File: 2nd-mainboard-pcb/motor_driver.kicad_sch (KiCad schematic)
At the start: 1 part

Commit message: added libraries
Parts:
- added J15: Stepper Motor, symbol Connector:Conn_01x04_Pin
- added J2: Servo Motor, symbol Connector:Conn_01x03_Socket
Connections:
- net GND: now reaches A1.1 (GND)
- net GND: now also A1.7 (GND)
- net +5V: now reaches A1.13 (~{RST})
- net +5V: now also A1.14 (~{SLP})
- net STEP: now reaches A1.15 (STEP)
- net DIR: now reaches A1.16 (DIR)
- net at A1.3 (A2): now also J15.3 (Pin_3)
- net at A1.4 (A1): now also J15.4 (Pin_4)
- net at A1.5 (B1): now also J15.2 (Pin_2)
- net at A1.6 (B2): now also J15.1 (Pin_1)
- net +12V: now reaches A1.8 (VMOT)
- no-connect marks 0 -> 2

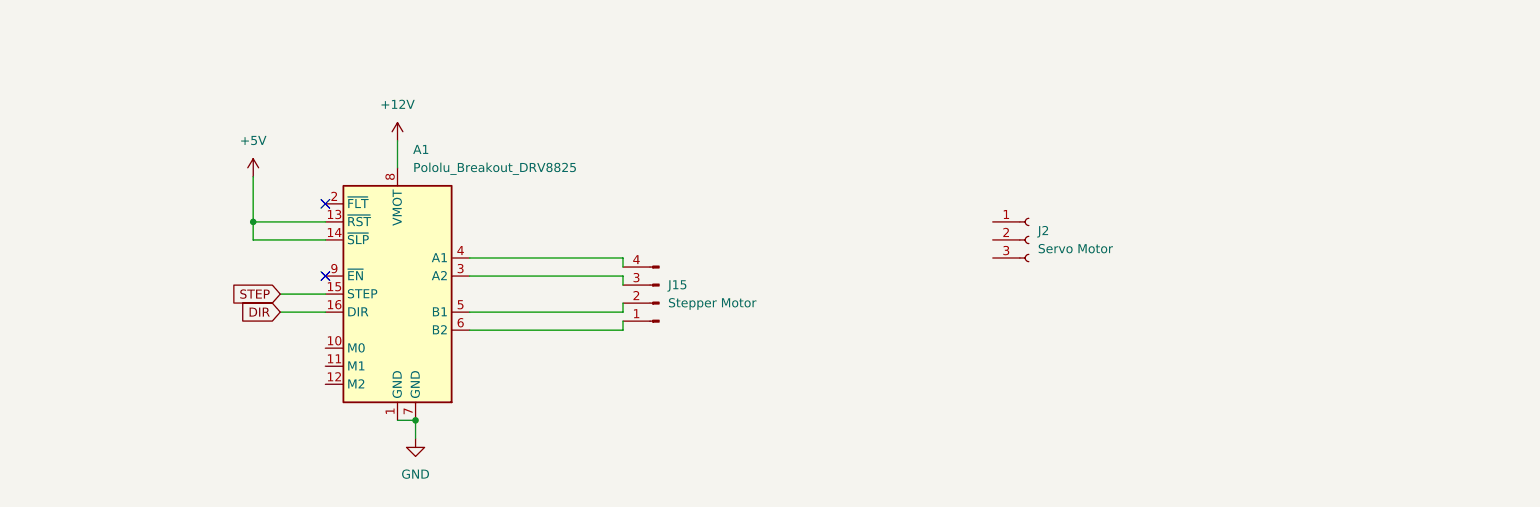
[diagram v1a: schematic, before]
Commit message: added imported components, changed structure
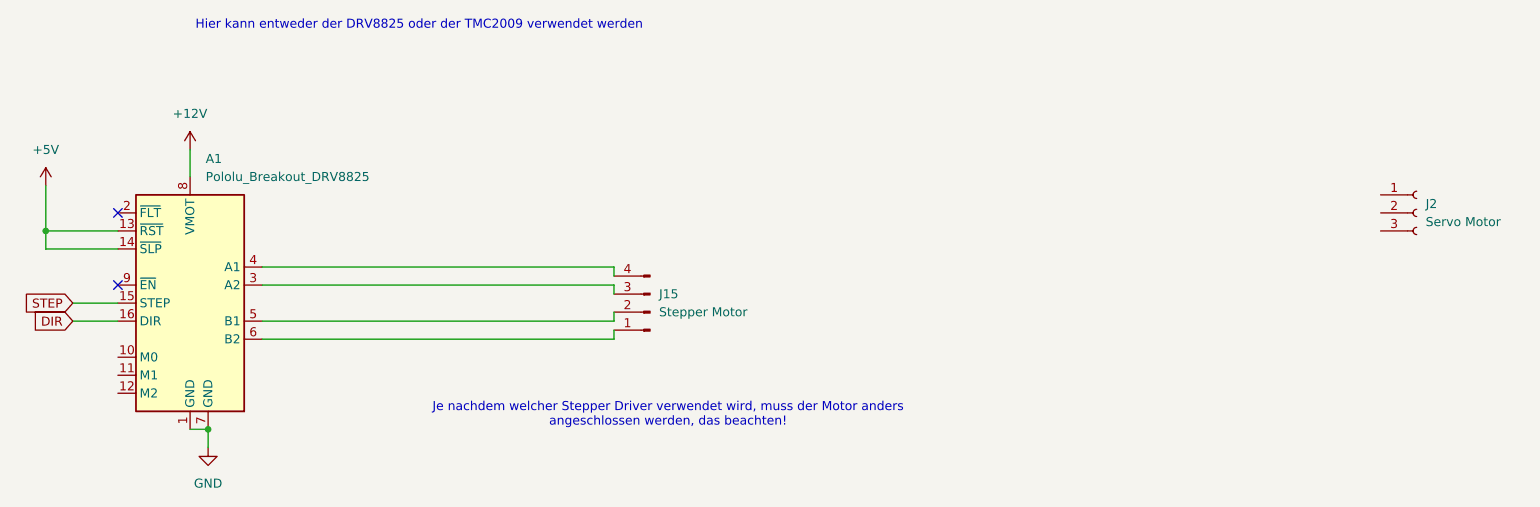
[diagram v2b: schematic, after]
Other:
- note added: "Hier kann entweder der DRV8825 oder der TMC2009 verwendet werden"
- note added: "Je nachdem welcher Stepper Driver verwendet wird, muss der Motor anders angeschlossen werden, das beachten!"
- moved on the sheet: A1, J15, J2

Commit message: Excel überarbeitet
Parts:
- added U4: MPU-6050, Sensor_Motion:InvenSense_QFN-24_4x4mm_P0.5mm, symbol Sensor_Motion:MPU-6050
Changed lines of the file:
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@@
+	)
+	(symbol
+		(lib_id "Sensor_Motion:MPU-6050")
+		(at 62.3888 139.1598 0)
+		(unit 1)
+		(exclude_from_sim no)
+		(in_bom yes)
+		(on_board yes)
+		(dnp no)
+		(fields_autoplaced yes)
+		(property "Reference" "U4"
+			(at 64.5829 155.6698 0)
+			(effects
+				(font
+					(size 1.27 1.27)
+				)
+				(justify left)
+			)
+		)
+		(property "Value" "MPU-6050"
+			(at 64.5829 158.2098 0)
+			(effects
+				(font
+					(size 1.27 1.27)
+				)
+				(justify left)
+			)
+		)
+		(property "Footprint" "Sensor_Motion:InvenSense_QFN-24_4x4mm_P0.5mm"
+			(at 62.3888 159.4798 0)
+			(effects
+				(font
+					(size 1.27 1.27)
+				)
+				(hide yes)
+			)
+		)
+		(property "Datasheet" "https://invensense.tdk.com/wp-content/uploads/2015/02/MPU-6000-Datasheet1.pdf"
+			(at 62.3888 142.9698 0)
+			(effects
+				(font
+					(size 1.27 1.27)
+				)
+				(hide yes)
+			)
+		)
+		(property "Description" "InvenSense 6-Axis Motion Sensor, Gyroscope, Accelerometer, I2C"
+			(at 62.3888 139.1598 0)
+			(effects
+				(font
+					(size 1.27 1.27)
+				)
+				(hide yes)
+			)
+		)
+		(pin "10"
+		)
+		(pin "14"
+		)
+		(pin "18"
+		)
+		(pin "20"
+		)
+		(pin "4"
+		)
+		(pin "5"
+		)
+		(pin "9"
+		)
+		(pin "12"
+		)
+		(pin "17"
+		)
+		(pin "2"
+		)
+		(pin "19"
+		)
+		(pin "7"
+		)
+		(pin "13"
+		)
+		(pin "24"
+		)
+		(pin "11"
+		)
+		(pin "3"
+		)
+		(pin "21"
+		)
+		(pin "8"
+		)
+		(pin "16"
+		)
+		(pin "22"
+		)
+		(pin "6"
+		)
+		(pin "1"
+		)
+		(pin "15"
+		)
+		(pin "23"
+		)
+		(instances
+			(project "2nd-mainboard-pcb"
+				(path "/6926a609-8b92-4b3a-88c8-3d023174b977/14240b98-f570-417b-af10-6e4a6547c4a4"
+					(reference "U4")
+					(unit 1)
+				)
+			)
+		)
 	)
 	(symbol

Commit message: finished stacked design, annotaded
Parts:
- removed J2: Servo Motor, symbol Connector:Conn_01x03_Socket
- added C27, C29, C31: 100nF, symbol Device:C
- added C28, C30: 4.7uF, symbol Device:C_Polarized
- added J12: Microstepping, symbol Connector_Generic:Conn_02x03_Counter_Clockwise
- added J14: Servo Motor SM, Imported_Component_Footprints:JST_XH_S3B-XH-A_1x03_P2.50mm_Horizontal, symbol Connector:Conn_01x03_Pin
- added J15: Servo Motor BL Touch, symbol Connector:Conn_01x03_Pin
- added J16: Conn_01x02_Pin, symbol Connector:Conn_01x02_Pin
- added U12: TMC2209_SILENTSTEPSTICK, Imported_Component_Footprints:MODULE_TMC2209_SILENTSTEPSTICK, symbol Imported_Component_Symbols:TMC2209_SILENTSTEPSTICK
- J13: renamed from J15; footprint (none) -> Imported_Component_Footprints:JST_S4B-XH-A-1
- renumbered U4 to U11
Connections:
- net +12V: now also U12.8 (VM)
- net DIR: now also U12.9 (DIR)
- net GND: now also U11.18 (GND), C27.2, C28.2, C29.2, C30.2, C31.2, J16.1 (Pin_1), U12.1 (GND), U12.7 (GND)
- net STEP: now also U12.10 (STEP)
- net M0: now reaches A1.10 (M0)
- net M0: now also J12.6 (Pin_6)
- net M1: now reaches A1.11 (M1)
- net M1: now also J12.5 (Pin_5), U12.15 (MS1)
- net M2: now reaches A1.12 (M2)
- net M2: now also J12.4 (Pin_4), U12.14 (MS2)
- net STP_A2: now reaches A1.3 (A2), J13.3 (Pin_3)
- net STP_A2: now also U12.5 (M2A)
- net STP_A1: now reaches A1.4 (A1), J13.4 (Pin_4)
- net STP_A1: now also U12.4 (M1A)
- net STP_B1: now reaches A1.5 (B1), J13.2 (Pin_2)
- net STP_B1: now also U12.3 (M1B)
- net STP_B2: now reaches A1.6 (B2), J13.1 (Pin_1)
- net STP_B2: now also U12.6 (M2B)
- net +5V_POW: now reaches U11.13 (VDD)
- net +5V_POW: now also U11.8 (VLOGIC), C27.1, C28.1, C29.1, C30.1, C31.1, J12.1 (Pin_1), J12.2 (Pin_2), J12.3 (Pin_3), J14.2 (Pin_2), J15.2 (Pin_2), U12.2 (VIO)
- net SCL: now reaches U11.23 (SCL)
- net SDA: now reaches U11.24 (SDA)
- new net BLT_Servo: J15.3 (Pin_3)
- new net BLT_Switch: J16.2 (Pin_2)
- new net SM_Servo: J14.3 (Pin_3)
- no-connect marks 2 -> 13
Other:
- note added: "Microstepping mit einem Jumper auf der Platine einstellen"
- note added: "Pinout https://www.studiopieters.nl/drv8825-pinout/"
- note added: "Welcher Pin muss zu UART verbunden werden?! https://www.ic-components.com/blog/your-guide-to-tmc2209-stepper-driver-with-microcontroller.jsp"
- moved on the sheet: J13, U11

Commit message: alle bauteile hinzugefügt
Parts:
- removed J12: Microstepping, symbol Connector_Generic:Conn_02x03_Counter_Clockwise
- added C28, C31: 100nF, Capacitor_SMD:C_0402_1005Metric_Pad0.74x0.62mm_HandSolder, symbol Device:C
- added J14: Microstepping, Imported_Component_Footprints:FTSH-103-01-L-DH, symbol Imported_Component_Symbols:FTSH-103-01-L-DH
- C29: renamed from C28; footprint (none) -> Capacitor_SMD:C_0805_2012Metric_Pad1.18x1.45mm_HandSolder
- C30: renamed from C29; footprint (none) -> Capacitor_SMD:C_0402_1005Metric_Pad0.74x0.62mm_HandSolder
- C32: renamed from C30; footprint (none) -> Capacitor_SMD:C_0805_2012Metric_Pad1.18x1.45mm_HandSolder
- C33: renamed from C31; footprint (none) -> Capacitor_SMD:C_0402_1005Metric_Pad0.74x0.62mm_HandSolder
- C34: renamed from C27; footprint (none) -> Capacitor_SMD:C_0402_1005Metric_Pad0.74x0.62mm_HandSolder
- J13: renamed from J15; now left out of the parts list
- J15: renamed from J16; now left out of the parts list
- U11: renamed from U12; now left out of the parts list
- renumbered J14 to J11, J13 to J12, U11 to U12
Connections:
- net +5V is gone; now on net +5V_POW: A1.13 (~{RST}), A1.14 (~{SLP})
- net +12V: now also C28.1
- net +5V_POW: now also C31.1, J14.01, J14.03, J14.05
- net GND: now also J11.1 (Pin_1), J13.1 (Pin_1), C28.2, C31.2
- net M0: now also J14.02
- net M1: now also J14.04
- net M2: now also J14.06
- net STP_A1: no longer U11.4 (M1A)
- net STP_A2: no longer U11.5 (M2A)
- net STP_B1: no longer U11.3 (M1B)
- net STP_B2: no longer U11.6 (M2B)
- no-connect marks 13 -> 24
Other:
- moved on the sheet: C34, U12

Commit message: mehr positioning
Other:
- moved on the sheet: C29, C30, C34, J11, J12, J14, U12

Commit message: Fan-PCB-Beginning
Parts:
- renumbered C28 to C23, C31 to C24, C29 to C25, C30 to C26, C34 to C27, C32 to C28, C33 to C29, J13 to J10, J15 to J11, J12 to J7, J11 to J8, J14 to J9

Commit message: Motoren Design finished
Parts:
- removed J11: Conn_01x02_Pin, symbol Connector:Conn_01x02_Pin
- added J11: T3, Imported_Component_Footprints:665102131822, symbol Imported_Component_Symbols:665102131822
- C28, C29: now fitted
- J10: footprint (none) -> Imported_Component_Footprints:JST_XH_S3B-XH-A_1x03_P2.50mm_Horizontal; now fitted; now in the parts list
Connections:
- net BLT_Switch: now also J11.2
- net GND: now also J11.1
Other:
- note added: "BL Touch Endschalter"
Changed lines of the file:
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@@
 		)
 	)
+	(text "BL Touch Endschalter"
+		(exclude_from_sim no)
+		(at 260.858 147.828 0)
+		(effects
+			(font
+				(size 1.27 1.27)
+			)
+		)
+	)
 	(global_label "M2"
 		(shape input)
@@
 		(in_bom yes)
 		(on_board yes)
-		(dnp yes)
+		(dnp no)
 		(fields_autoplaced yes)
 		(property "Reference" "#PWR067"
@@
 		(in_bom yes)
 		(on_board yes)
-		(dnp yes)
+		(dnp no)
 		(fields_autoplaced yes)
 		(property "Reference" "C29"
@@
 	)
 	(symbol
+		(lib_id "Imported_Component_Symbols:665102131822")
+		(at 251.46 153.67 270)
+		(unit 1)
+		(exclude_from_sim no)
+		(in_bom yes)
+		(on_board yes)
+		(dnp no)
+		(fields_autoplaced yes)
+		(property "Reference" "J11"
+			(at 252.73 152.3999 90)
+			(effects
+				(font
+					(size 1.27 1.27)
+				)
+				(justify left)
+			)
+		)
+		(property "Value" "T3"
+			(at 260.604 153.924 0)
+			(effects
+				(font
+					(size 1.27 1.27)
+				)
+				(justify bottom)
+				(hide yes)
+			)
+		)
+		(property "Footprint" "Imported_Component_Footprints:665102131822"
+			(at 260.604 153.924 0)
+			(effects
+				(font
+					(size 1.27 1.27)
+				)
+				(justify bottom)
+				(hide yes)
+			)
+		)
+		(property "Datasheet" ""
+			(at 251.46 153.67 0)
+			(effects
+				(font
+					(size 1.27 1.27)
+				)
+				(hide yes)
+			)
+		)
+		(property "Description" ""
+			(at 251.46 153.67 0)
+			(effects
+				(font
+					(size 1.27 1.27)
+				)
+				(hide yes)
+			)
+		)
+		(property "CONTACT-RESISTANCE" "20mOhm"
+			(at 260.604 153.924 0)
+			(effects
+				(font
+					(size 1.27 1.27)
+				)
+				(justify bottom)
+				(hide yes)
+			)
+		)
+		(property "GENDER" "Male"
+			(at 260.604 153.924 0)
+			(effects
+				(font
+					(size 1.27 1.27)
+				)
+				(justify bottom)
+				(hide yes)
+			)
+		)
+		(property "MOUNT" "SMT"
+			(at 254.254 153.416 0)
+			(effects
+				(font
+					(size 1.27 1.27)
+				)
+				(justify bottom)
+				(hide yes)
+			)
+		)
+		(property "IR" "1A"
+			(at 252.73 157.988 0)
+			(effects
+				(font
+					(size 1.27 1.27)
+				)
+				(justify bottom)
+				(hide yes)
+			)
+		)
+		(property "L" "4mm"
+			(at 260.604 153.924 0)
+			(effects
+				(font
+					(size 1.27 1.27)
+				)
+				(justify bottom)
+				(hide yes)
+			)
+		)
+		(property "PACKAGING" "Tape and Reel"
+			(at 260.604 153.924 0)
+			(effects
+				(font
+					(size 1.27 1.27)
+				)
+				(justify bottom)
+				(hide yes)
+			)
+		)
+		(property "PART-NUMBER" "665102131822"
+			(at 260.604 153.924 0)
+			(effects
+				(font
+					(size 1.27 1.27)
+				)
+				(justify bottom)
+				(hide yes)
+			)
+		)
+		(property "DATASHEET-URL" "https://www.we-online.com/redexpert/spec/665102131822?ae"
+			(at 255.778 149.352 0)
+			(effects
+				(font
+					(size 1.27 1.27)
+				)
+				(justify bottom)
+				(hide yes)
+			)
+		)
+		(property "WORKING-VOLTAGE" "50V(AC)"
+			(at 260.604 153.924 0)
+			(effects
+				(font
+					(size 1.27 1.27)
+				)
+				(justify bottom)
+				(hide yes)
+			)
+		)
+		(property "PINS" "2"
+			(at 253.238 150.368 0)
+			(effects
+				(font
+					(size 1.27 1.27)
+				)
+				(justify bottom)
+				(hide yes)
+			)
+		)
+		(property "PITCH" "1mm"
+			(at 260.604 153.924 0)
+			(effects
+				(font
+					(size 1.27 1.27)
+				)
+				(justify bottom)
+				(hide yes)
+			)
+		)
+		(property "TYPE" "Horizontal"
+			(at 260.604 153.924 0)
+			(effects
+				(font
+					(size 1.27 1.27)
+				)
+				(justify bottom)
+				(hide yes)
+			)
+		)
+		(property "PCB-CABLE-PANEL" "PCB"
+			(at 252.222 153.67 0)
+			(effects
+				(font
+					(size 1.27 1.27)
+				)
+				(justify bottom)
+				(hide yes)
+			)
+		)
+		(pin "1"
+		)
+		(pin "2"
+		)
+		(instances
+			(project "2nd-mainboard-pcb"
+				(path "/6926a609-8b92-4b3a-88c8-3d023174b977/14240b98-f570-417b-af10-6e4a6547c4a4"
+					(reference "J11")
+					(unit 1)
+				)
+			)
+		)
+	)
+	(symbol
 		(lib_id "Connector:Conn_01x03_Pin")
 		(at 251.46 123.19 180)
 		(unit 1)
 		(exclude_from_sim no)
-		(in_bom no)
-		(on_board no)
-		(dnp yes)
+		(in_bom yes)
+		(on_board yes)
+		(dnp no)
 		(property "Reference" "J10"
 			(at 252.73 121.9199 0)
@@
 			)
 		)
-		(property "Footprint" ""
+		(property "Footprint" "Imported_Component_Footprints:JST_XH_S3B-XH-A_1x03_P2.50mm_Horizontal"
 			(at 251.46 123.19 0)
 			(effects
@@
 		(in_bom yes)
 		(on_board yes)
-		(dnp yes)
+		(dnp no)
 		(property "Reference" "#PWR066"
 			(at 203.2 143.51 0)
@@
 	)
 	(symbol
-		(lib_id "Connector:Conn_01x02_Pin")
-		(at 251.46 153.67 180)
-		(unit 1)
-		(exclude_from_sim no)
-		(in_bom no)
-		(on_board no)
-		(dnp yes)
-		(fields_autoplaced yes)
-		(property "Reference" "J11"
-			(at 252.73 151.1299 0)
-			(effects
-				(font
-					(size 1.27 1.27)
-				)
-				(justify right)
-			)
-		)
-		(property "Value" "Conn_01x02_Pin"
-			(at 252.73 153.6699 0)
-			(effects
-				(font
-					(size 1.27 1.27)
-				)
-				(justify right)
-			)
-		)
-		(property "Footprint" ""
-			(at 251.46 153.67 0)
-			(effects
-				(font
-					(size 1.27 1.27)
-				)
-				(hide yes)
-			)
-		)
-		(property "Datasheet" "~"
-			(at 251.46 153.67 0)
-			(effects
-				(font
-					(size 1.27 1.27)
-				)
-				(hide yes)
-			)
-		)
-		(property "Description" "Generic connector, single row, 01x02, script generated"
-			(at 251.46 153.67 0)
-			(effects
-				(font
-					(size 1.27 1.27)
-				)
-				(hide yes)
-			)
-		)
-		(pin "1"
-		)
-		(pin "2"
-		)
-		(instances
-			(project ""
-				(path "/6926a609-8b92-4b3a-88c8-3d023174b977/14240b98-f570-417b-af10-6e4a6547c4a4"
-					(reference "J11")
-					(unit 1)
-				)
-			)
-		)
-	)
-	(symbol
 		(lib_id "power:+5VP")
 		(at 203.2 121.92 0)
@@
 		(in_bom yes)
 		(on_board yes)
-		(dnp yes)
+		(dnp no)
 		(fields_autoplaced yes)
 		(property "Reference" "#PWR063"
@@
 		(in_bom yes)
 		(on_board yes)
-		(dnp yes)
+		(dnp no)
 		(fields_autoplaced yes)
 		(property "Reference" "C28"
@@
 		(in_bom yes)
 		(on_board yes)
-		(dnp yes)
+		(dnp no)
 		(fields_autoplaced yes)
 		(property "Reference" "#PWR068"
